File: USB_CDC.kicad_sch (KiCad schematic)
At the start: 4 parts, among them P1 USB_C_Plug_USB2.0

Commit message: added user ports
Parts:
- 5.1K2, R2: footprint (none) -> Resistor_SMD:R_0805_2012Metric_Pad1.20x1.40mm_HandSolder
- C23: footprint (none) -> Capacitor_SMD:C_0805_2012Metric_Pad1.18x1.45mm_HandSolder
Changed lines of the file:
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@@
 			)
 		)
-		(property "Footprint" ""
+		(property "Footprint" "Capacitor_SMD:C_0805_2012Metric_Pad1.18x1.45mm_HandSolder"
 			(at 113.9952 116.84 0)
 			(hide yes)
@@
 			)
 		)
-		(property "Footprint" ""
+		(property "Footprint" "Resistor_SMD:R_0805_2012Metric_Pad1.20x1.40mm_HandSolder"
 			(at 102.362 113.03 90)
 			(hide yes)
@@
 			)
 		)
-		(property "Footprint" ""
+		(property "Footprint" "Resistor_SMD:R_0805_2012Metric_Pad1.20x1.40mm_HandSolder"
 			(at 152.4 77.978 90)
 			(hide yes)

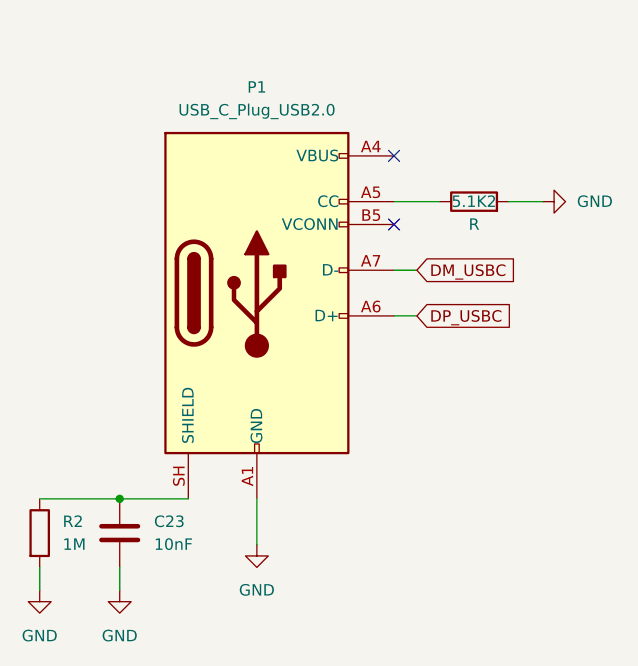
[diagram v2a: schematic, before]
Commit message: added 5v buck converter and place JST PH connectors
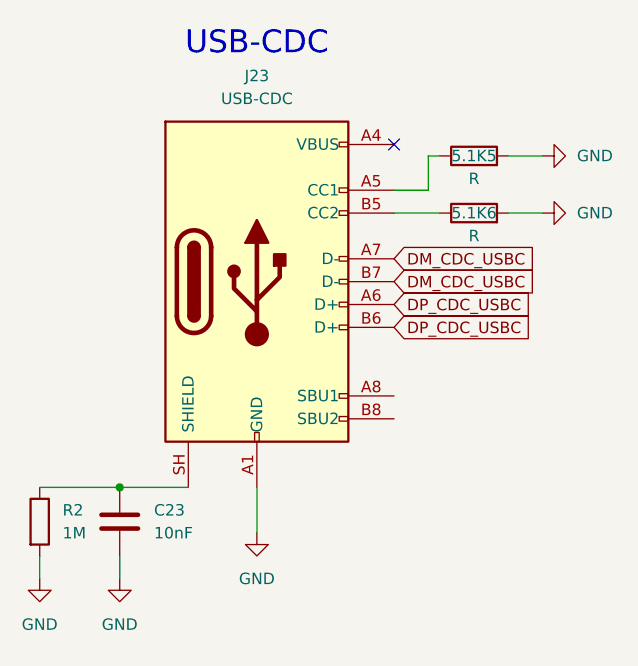
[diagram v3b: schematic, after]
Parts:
- removed 5.1K2: R, Resistor_SMD:R_0805_2012Metric_Pad1.20x1.40mm_HandSolder, symbol Device:R
- removed P1: USB_C_Plug_USB2.0, Connector_USB:USB_C_Receptacle_HRO_TYPE-C-31-M-12, symbol Connector:USB_C_Plug_USB2.0
- added 5.1K5, 5.1K6: R, Resistor_SMD:R_0805_2012Metric_Pad1.20x1.40mm_HandSolder, symbol Device:R
- added J23: USB-CDC, Connector_USB:USB_C_Receptacle_HRO_TYPE-C-31-M-12, symbol Connector:USB_C_Receptacle_USB2.0_16P
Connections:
- net GND: now also 5.1K5.2, 5.1K6.2, J23.A1 (GND), J23.A12 (GND), J23.B1 (GND), J23.B12 (GND)
- net at C23.1, R2.1: now also J23.SH (SHIELD)
- new net: 5.1K5.1, J23.A5 (CC1)
- new net: 5.1K6.1, J23.B5 (CC2)
- new net: J23.A4 (VBUS), J23.A9 (VBUS), J23.B4 (VBUS), J23.B9 (VBUS)
- new net DM_CDC_USBC: J23.A7 (D-), J23.B7 (D-)
- new net DP_CDC_USBC: J23.A6 (D+), J23.B6 (D+)
- no-connect marks 2 -> 1
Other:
- note added: "USB-CDC"
- moved on the sheet: C23, R2

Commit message: fix 5v_buck scheme and delete bad name scheme
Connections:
- no-connect marks 1 -> 3
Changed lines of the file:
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@@
+	)
+	(no_connect
+		(at 143.51 100.33)
 	)
 	(no_connect
 		(at 143.51 69.85)
 	)
+	(no_connect
+		(at 143.51 97.79)
+	)
 	(wire
